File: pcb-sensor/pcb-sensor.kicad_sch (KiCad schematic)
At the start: 28 parts, among them J1 Conn_02x06_Counter_Clockwise, J2 Conn_01x03, J3 Conn_01x01, J4 Conn_01x05, J5 Conn_01x02, J6 Conn_01x03, J7 Conn_01x01, J8 Conn_01x01, U1 LM340MP, U2 SFH617A-1, U4 SFH617A-1

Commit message: resolves #37: optocoupler footprint
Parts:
- U2, U4: value SFH617A-1 -> SFH617A-2X009T; footprint Package_SO:SOP-4_4.4x2.6mm_P1.27mm -> Package_DIP:SMDIP-4_W7.62mm; symbol Isolator:SFH617A-1 -> Isolator:SFH617A-2X009T
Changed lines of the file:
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@@
     (pin "1")
   )
-  (symbol (lib_id "Isolator:SFH617A-1") (at 184.15 88.9 0) (unit 1)
+  (symbol (lib_id "Isolator:SFH617A-2X009T") (at 184.15 88.9 0) (unit 1)
     (in_bom yes) (on_board yes)
     (property "Reference" "U2" (id 0) (at 184.15 82.9818 0))
-    (property "Value" "SFH617A-1" (id 1) (at 184.15 93.98 0))
-    (property "Footprint" "Package_SO:SOP-4_4.4x2.6mm_P1.27mm" (id 2) (at 179.07 93.98 0)
-      (effects (font (size 1.27 1.27) italic) (justify left) hide)
-    )
-    (property "Datasheet" "http://www.vishay.com/docs/83740/sfh617a.pdf" (id 3) (at 184.15 88.9 0)
-      (effects (font (size 1.27 1.27)) (justify left) hide)
+    (property "Value" "SFH617A-2X009T" (id 1) (at 184.15 93.98 0))
+    (property "Footprint" "Package_DIP:SMDIP-4_W7.62mm" (id 2) (at 184.15 96.52 0)
+      (effects (font (size 1.27 1.27)) hide)
+    )
+    (property "Datasheet" "http://www.vishay.com/docs/83740/sfh617a.pdf" (id 3) (at 175.26 81.28 0)
+      (effects (font (size 1.27 1.27)) hide)
     )
     (pin "1")
@@
     (pin "4")
   )
-  (symbol (lib_id "Isolator:SFH617A-1") (at 251.46 90.17 0) (unit 1)
+  (symbol (lib_id "Isolator:SFH617A-2X009T") (at 251.46 90.17 0) (unit 1)
     (in_bom yes) (on_board yes)
     (property "Reference" "U4" (id 0) (at 251.46 84.2518 0))
-    (property "Value" "SFH617A-1" (id 1) (at 251.46 95.25 0))
-    (property "Footprint" "Package_SO:SOP-4_4.4x2.6mm_P1.27mm" (id 2) (at 246.38 95.25 0)
-      (effects (font (size 1.27 1.27) italic) (justify left) hide)
-    )
-    (property "Datasheet" "http://www.vishay.com/docs/83740/sfh617a.pdf" (id 3) (at 251.46 90.17 0)
-      (effects (font (size 1.27 1.27)) (justify left) hide)
+    (property "Value" "SFH617A-2X009T" (id 1) (at 251.46 95.25 0))
+    (property "Footprint" "Package_DIP:SMDIP-4_W7.62mm" (id 2) (at 251.46 97.79 0)
+      (effects (font (size 1.27 1.27)) hide)
+    )
+    (property "Datasheet" "http://www.vishay.com/docs/83740/sfh617a.pdf" (id 3) (at 242.57 82.55 0)
+      (effects (font (size 1.27 1.27)) hide)
     )
     (pin "1")
@@
     )
     (path "/00000000-0000-0000-0000-000061cdde7e"
-      (reference "U2") (unit 1) (value "SFH617A-1") (footprint "Package_SO:SOP-4_4.4x2.6mm_P1.27mm")
+      (reference "U2") (unit 1) (value "SFH617A-2X009T") (footprint "Package_DIP:SMDIP-4_W7.62mm")
     )
     (path "/00000000-0000-0000-0000-000061ceb6aa"
-      (reference "U4") (unit 1) (value "SFH617A-1") (footprint "Package_SO:SOP-4_4.4x2.6mm_P1.27mm")
-    )
-  )
+      (reference "U4") (unit 1) (value "SFH617A-2X009T") (footprint "Package_DIP:SMDIP-4_W7.62mm")
+    )
+  )

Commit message: resolves #43: reduce hall effect sensor pull up to remove noise
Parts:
- R11: value 10k -> 1k
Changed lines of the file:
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@@
       (effects (font (size 1.27 1.27)) (justify left))
     )
-    (property "Value" "10k" (id 1) (at 263.398 139.573 0)
+    (property "Value" "1k" (id 1) (at 263.398 139.573 0)
       (effects (font (size 1.27 1.27)) (justify left))
     )
@@
     )
     (path "/00000000-0000-0000-0000-0000616846c0"
-      (reference "R11") (unit 1) (value "10k") (footprint "Resistor_SMD:R_1206_3216Metric_Pad1.30x1.75mm_HandSolder")
+      (reference "R11") (unit 1) (value "1k") (footprint "Resistor_SMD:R_1206_3216Metric_Pad1.30x1.75mm_HandSolder")
     )
     (path "/00000000-0000-0000-0000-0000617d50e9"

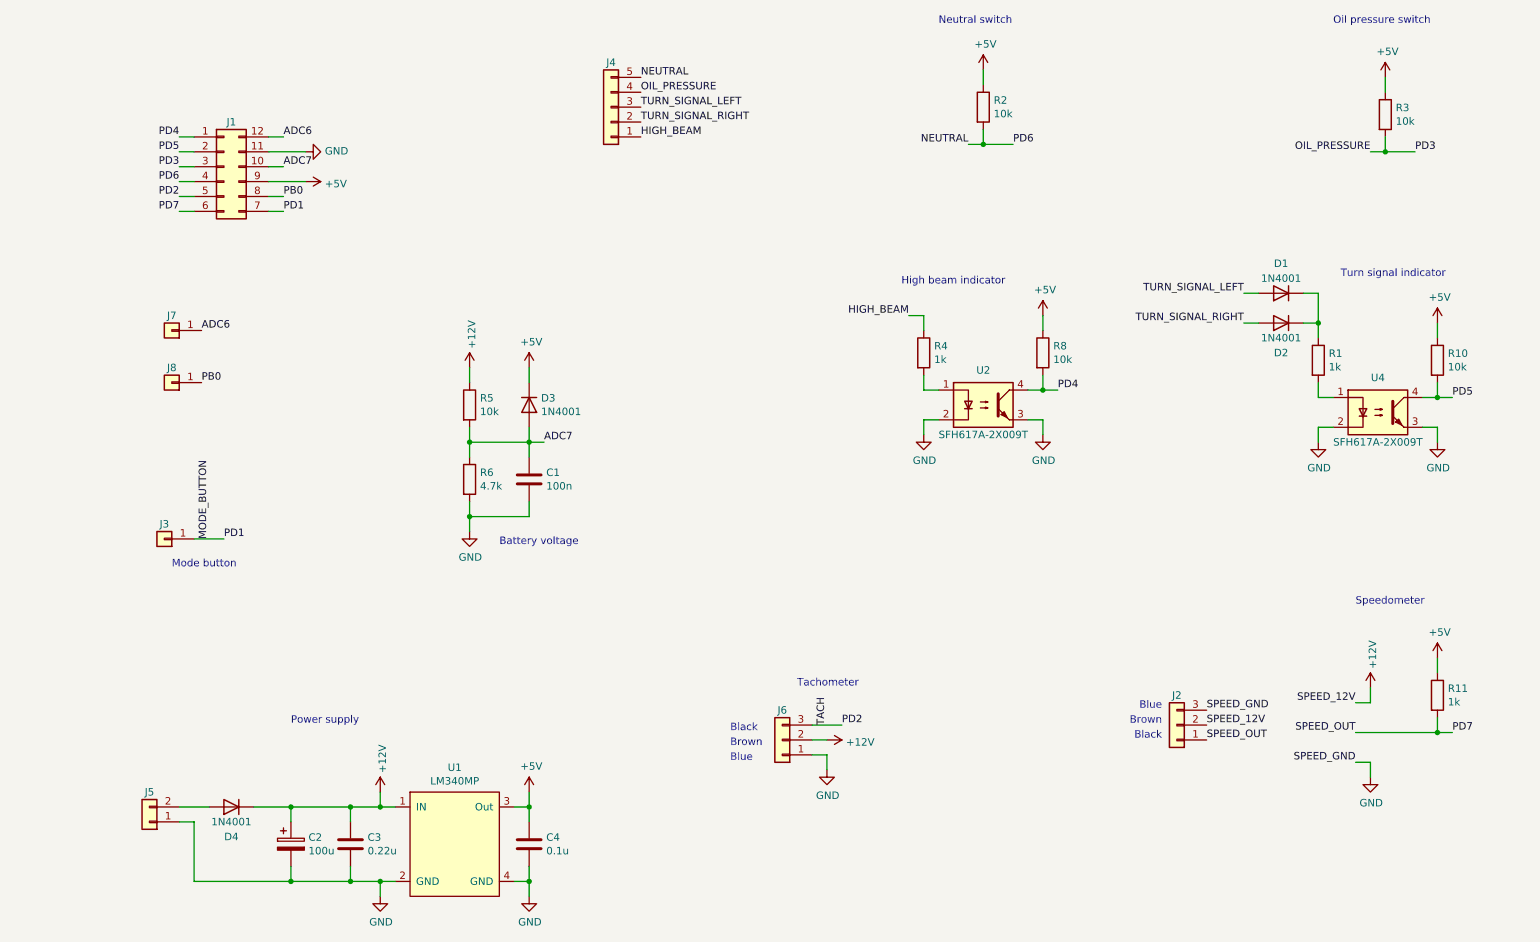
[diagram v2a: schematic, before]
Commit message: resolves #26: protection diodes
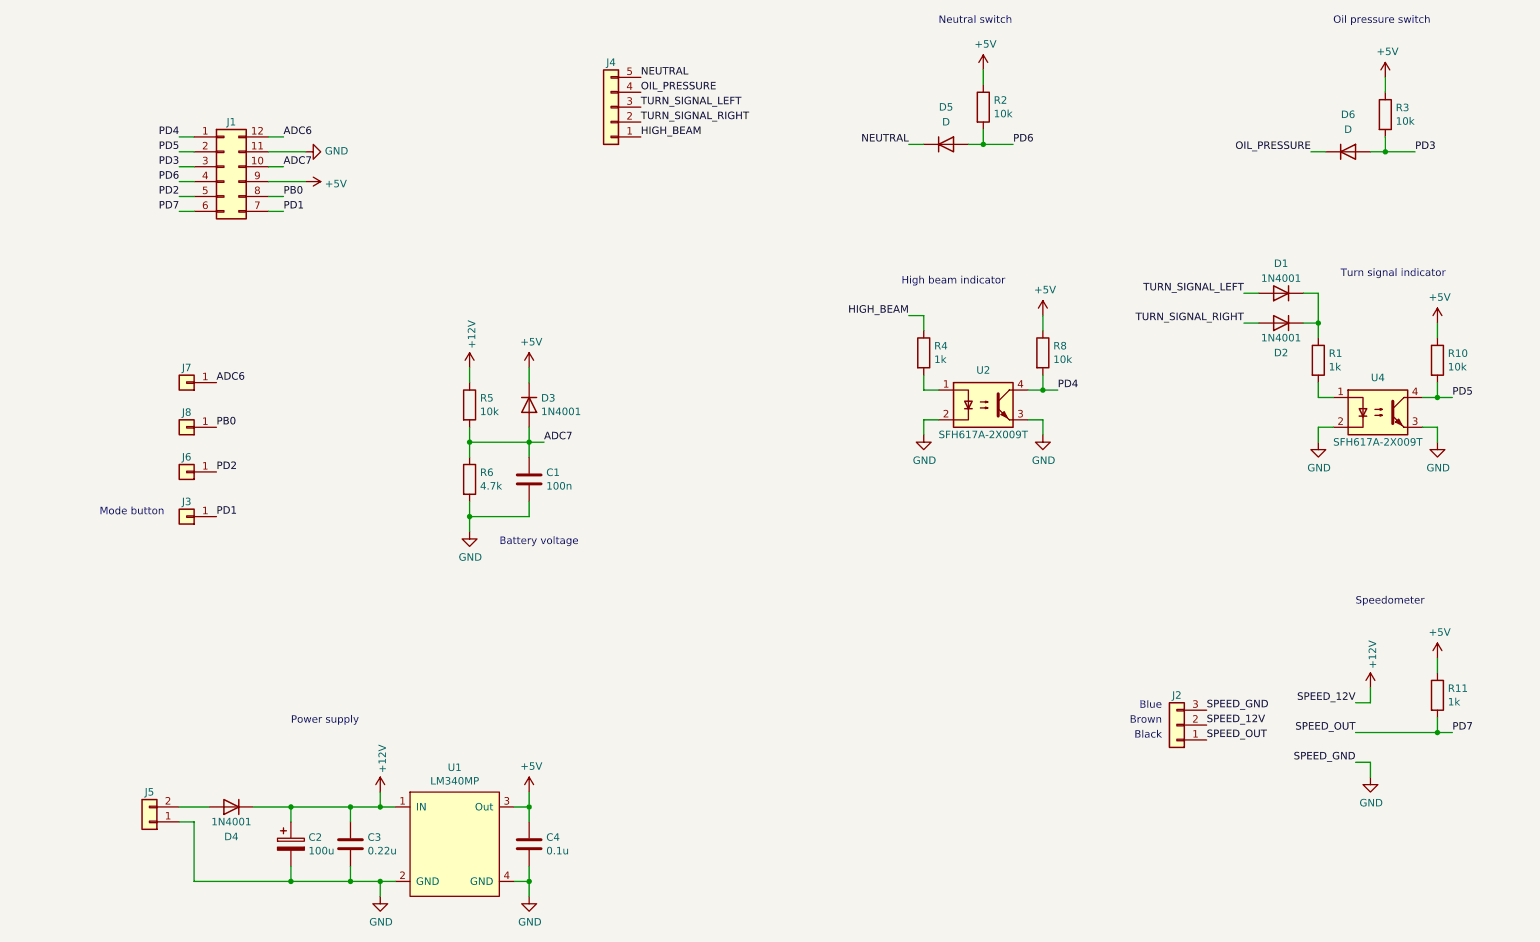
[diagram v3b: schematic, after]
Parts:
- removed J6: Conn_01x03, Connector_PinSocket_2.54mm:PinSocket_1x03_P2.54mm_Vertical, symbol Connector_Generic:Conn_01x03
- added D5, D6: D, Diode_SMD:D_1206_3216Metric_Pad1.42x1.75mm_HandSolder, symbol Device:D
- added J6: Conn_01x01, Connector_PinSocket_2.54mm:PinSocket_1x01_P2.54mm_Vertical, symbol Connector_Generic:Conn_01x01
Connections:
- net NEUTRAL: now also D5.1 (K); no longer J1.4 (Pin_4), R2.2
- net OIL_PRESSURE: now also D6.1 (K); no longer J1.3 (Pin_3), R3.2
- net PD2: now also J6.1 (Pin_1)
- net MODE_BUTTON renamed PD1
- new net PD3: D6.2 (A), J1.3 (Pin_3), R3.2
- new net PD6: D5.2 (A), J1.4 (Pin_4), R2.2
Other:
- note removed: "Tachometer"
- moved on the sheet: J3, J7, J8

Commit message: resolves #17: interrupt pin
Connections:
- net PD2: now also J2.1 (Pin_1), R11.2; no longer J6.1 (Pin_1)
- net PD7: now also J6.1 (Pin_1); no longer J2.1 (Pin_1), R11.2
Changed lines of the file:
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@@
     (effects (font (size 1.27 1.27)) (justify right bottom))
   )
-  (label "PD2" (at 53.34 100.33 0)
+  (label "PD7" (at 53.34 100.33 0)
     (effects (font (size 1.27 1.27)) (justify left bottom))
   )
@@
     (effects (font (size 1.27 1.27)) (justify right bottom))
   )
-  (label "PD7" (at 264.16 144.78 0)
+  (label "PD2" (at 264.16 144.78 0)
     (effects (font (size 1.27 1.27)) (justify left bottom))
   )

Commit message: resolves #46: mode button connector
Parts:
- removed J3: Conn_01x01, Connector_PinSocket_2.54mm:PinSocket_1x01_P2.54mm_Vertical, symbol Connector_Generic:Conn_01x01
- added J9: Conn_01x02_Male, Connector_JST:JST_PH_S2B-PH-K_1x02_P2.00mm_Horizontal, symbol Connector:Conn_01x02_Male
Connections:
- net GND: now also J9.2 (Pin_2)
- net PD1: now also J9.1 (Pin_1)
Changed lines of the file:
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@@
+    (stroke (width 0) (type default) (color 0 0 0 0))
+  )
+  (wire (pts (xy 154.94 132.08) (xy 157.48 132.08))
     (stroke (width 0) (type default) (color 0 0 0 0))
   )
@@
     (stroke (width 0) (type default) (color 0 0 0 0))
   )
+  (wire (pts (xy 154.94 134.62) (xy 157.48 134.62))
+    (stroke (width 0) (type default) (color 0 0 0 0))
+  )
   (text "Neutral switch" (at 176.53 24.13 0)
     (effects (font (size 1.27 1.27)) (justify left bottom))
@@
     (effects (font (size 1.27 1.27)) (justify left bottom))
   )
-  (text "Mode button" (at 44.45 107.95 180)
+  (text "Mode button" (at 156.21 139.7 180)
     (effects (font (size 1.27 1.27)) (justify right bottom))
   )
@@
     (effects (font (size 1.27 1.27)) (justify left bottom))
   )
-  (label "PD1" (at 53.34 107.95 0)
-    (effects (font (size 1.27 1.27)) (justify left bottom))
-  )
   (label "PD1" (at 64.77 55.88 0)
     (effects (font (size 1.27 1.27)) (justify left bottom))
@@
   (label "PD3" (at 46.99 48.26 180)
     (effects (font (size 1.27 1.27)) (justify right bottom))
+  )
+  (label "PD1" (at 157.48 132.08 0)
+    (effects (font (size 1.27 1.27)) (justify left bottom))
   )
   (symbol (lib_id "Connector_Generic:Conn_02x06_Counter_Clockwise") (at 54.61 48.26 0) (unit 1)
@@
     (pin "4")
   )
-  (symbol (lib_id "Connector_Generic:Conn_01x01") (at 48.26 107.95 180) (unit 1)
-    (in_bom yes) (on_board yes)
-    (property "Reference" "J3" (id 0) (at 48.26 105.41 0))
-    (property "Value" "Conn_01x01" (id 1) (at 50.3428 104.5464 0)
-      (effects (font (size 1.27 1.27)) hide)
-    )
-    (property "Footprint" "Connector_PinSocket_2.54mm:PinSocket_1x01_P2.54mm_Vertical" (id 2) (at 48.26 107.95 0)
-      (effects (font (size 1.27 1.27)) hide)
-    )
-    (property "Datasheet" "~" (id 3) (at 48.26 107.95 0)
-      (effects (font (size 1.27 1.27)) hide)
-    )
-    (pin "1")
-  )
   (symbol (lib_id "Connector_Generic:Conn_01x01") (at 48.26 92.71 180) (unit 1)
     (in_bom yes) (on_board yes)
@@
     (pin "2")
   )
+  (symbol (lib_id "power:GND") (at 157.48 134.62 90) (unit 1)
+    (in_bom yes) (on_board yes)
+    (property "Reference" "#PWR0105" (id 0) (at 163.83 134.62 0)
+      (effects (font (size 1.27 1.27)) hide)
+    )
+    (property "Value" "GND" (id 1) (at 160.7312 134.493 90)
+      (effects (font (size 1.27 1.27)) (justify right))
+    )
+    (property "Footprint" "" (id 2) (at 157.48 134.62 0)
+      (effects (font (size 1.27 1.27)) hide)
+    )
+    (property "Datasheet" "" (id 3) (at 157.48 134.62 0)
+      (effects (font (size 1.27 1.27)) hide)
+    )
+    (pin "1")
+  )
   (symbol (lib_id "Connector_Generic:Conn_01x01") (at 48.26 100.33 180) (unit 1)
     (in_bom yes) (on_board yes)
@@
     )
     (pin "1")
+  )
+  (symbol (lib_id "Connector:Conn_01x02_Male") (at 149.86 132.08 0) (unit 1)
+    (in_bom yes) (on_board yes) (fields_autoplaced)
+    (property "Reference" "J9" (id 0) (at 150.495 127 0))
+    (property "Value" "Conn_01x02_Male" (id 1) (at 150.495 129.54 0))
+    (property "Footprint" "Connector_JST:JST_PH_S2B-PH-K_1x02_P2.00mm_Horizontal" (id 2) (at 149.86 132.08 0)
+      (effects (font (size 1.27 1.27)) hide)
+    )
+    (property "Datasheet" "~" (id 3) (at 149.86 132.08 0)
+      (effects (font (size 1.27 1.27)) hide)
+    )
+    (pin "1")
+    (pin "2")
   )
   (sheet_instances
@@
       (reference "#PWR0104") (unit 1) (value "+12V") (footprint "")
     )
+    (path "/8fc9b42a-be9e-4b68-b6b5-47e33fba5f6c"
+      (reference "#PWR0105") (unit 1) (value "GND") (footprint "")
+    )
     (path "/00000000-0000-0000-0000-00006187b8d1"
       (reference "#PWR0106") (unit 1) (value "GND") (footprint "")
@@
       (reference "J2") (unit 1) (value "Conn_01x03") (footprint "Connector_PinSocket_2.54mm:PinSocket_1x03_P2.54mm_Vertical")
     )
-    (path "/00000000-0000-0000-0000-000061df2613"
-      (reference "J3") (unit 1) (value "Conn_01x01") (footprint "Connector_PinSocket_2.54mm:PinSocket_1x01_P2.54mm_Vertical")
-    )
     (path "/00000000-0000-0000-0000-000061af42fb"
       (reference "J4") (unit 1) (value "Conn_01x05") (footprint "Connector_PinSocket_2.54mm:PinSocket_1x05_P2.54mm_Vertical")
@@
       (reference "J8") (unit 1) (value "Conn_01x01") (footprint "Connector_PinSocket_2.54mm:PinSocket_1x01_P2.54mm_Vertical")
     )
+    (path "/e17ef7e8-7ef3-48c9-a4ab-39b37df20ec3"
+      (reference "J9") (unit 1) (value "Conn_01x02_Male") (footprint "Connector_JST:JST_PH_S2B-PH-K_1x02_P2.00mm_Horizontal")
+    )
     (path "/00000000-0000-0000-0000-0000618559fe"

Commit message: update layout
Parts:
- removed J2: Conn_01x03, Connector_PinSocket_2.54mm:PinSocket_1x03_P2.54mm_Vertical, symbol Connector_Generic:Conn_01x03
- removed J4: Conn_01x05, Connector_PinSocket_2.54mm:PinSocket_1x05_P2.54mm_Vertical, symbol Connector_Generic:Conn_01x05
- removed J5: Conn_01x02, Connector_PinSocket_2.54mm:PinSocket_1x02_P2.54mm_Vertical, symbol Connector_Generic:Conn_01x02
- removed J6, J7, J8: Conn_01x01, Connector_PinSocket_2.54mm:PinSocket_1x01_P2.54mm_Vertical, symbol Connector_Generic:Conn_01x01
- removed J9: Conn_01x02_Male, Connector_JST:JST_PH_S2B-PH-K_1x02_P2.00mm_Horizontal, symbol Connector:Conn_01x02_Male
- added J2, J5: Conn_01x02_Male, Connector_JST:JST_PH_S2B-PH-K_1x02_P2.00mm_Horizontal, symbol Connector:Conn_01x02_Male
- added J3, J6: Conn_01x03_Male, Connector_JST:JST_PH_S3B-PH-K_1x03_P2.00mm_Horizontal, symbol Connector:Conn_01x03_Male
- added J4: Conn_01x05_Male, Connector_JST:JST_PH_S5B-PH-K_1x05_P2.00mm_Horizontal, symbol Connector:Conn_01x05_Male
- added R7: 47k, Resistor_SMD:R_1206_3216Metric_Pad1.30x1.75mm_HandSolder, symbol Device:R
- added R9: 1k, Resistor_SMD:R_1206_3216Metric_Pad1.30x1.75mm_HandSolder, symbol Device:R
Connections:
- net +12V: now also J3.1 (Pin_1), J6.1 (Pin_1)
- net +5V: now also R7.1, R9.1
- net ADC6: now also J2.1 (Pin_1), R7.2
- net GND: now also J2.2 (Pin_2), J3.3 (Pin_3), J5.2 (Pin_2), J6.3 (Pin_3)
- net HIGH_BEAM: now also J4.5 (Pin_5)
- net NEUTRAL: now also J4.1 (Pin_1)
- net OIL_PRESSURE: now also J4.2 (Pin_2)
- net PD1: now also D6.2 (A), R3.2
- net PD2: now also J6.2 (Pin_2)
- net PD3: now also J3.2 (Pin_2), R9.2; no longer D6.2 (A), R3.2
- net TURN_SIGNAL_LEFT: now also J4.3 (Pin_3)
- net TURN_SIGNAL_RIGHT: now also J4.4 (Pin_4)
- net at D4.2 (A): now also J5.1 (Pin_1)
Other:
- note added: "Tachometer"
- note added: "Temperature"
- note removed: "Mode button"
- moved on the sheet: C1, C2, C3, C4, D1, D2, D3, D4, D5, J1, R1, R10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

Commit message: update pcb layouts
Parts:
- removed J2, J5: Conn_01x02_Male, Connector_JST:JST_PH_S2B-PH-K_1x02_P2.00mm_Horizontal, symbol Connector:Conn_01x02_Male
- removed J3, J6: Conn_01x03_Male, Connector_JST:JST_PH_S3B-PH-K_1x03_P2.00mm_Horizontal, symbol Connector:Conn_01x03_Male
- removed J4: Conn_01x05_Male, Connector_JST:JST_PH_S5B-PH-K_1x05_P2.00mm_Horizontal, symbol Connector:Conn_01x05_Male
- added J7: Conn_02x08_Top_Bottom, Connector_Molex:Molex_Mini-Fit_Jr_5566-16A_2x08_P4.20mm_Vertical, symbol Connector_Generic:Conn_02x08_Top_Bottom
- J1: footprint Connector_PinSocket_2.54mm:PinSocket_2x06_P2.54mm_Vertical -> Connector_PinSocket_2.00mm:PinSocket_2x06_P2.00mm_Vertical
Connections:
- net +12V: now also J7.4 (Pin_4), J7.6 (Pin_6)
- net ADC6: now also C1.1, D3.2 (A), R5.2, R6.1; no longer R7.2
- net ADC7: now also R7.2, J7.2 (Pin_2); no longer C1.1, D3.2 (A), R5.2, R6.1
- net GND: now also J7.1 (Pin_1), J7.10 (Pin_10), J7.11 (Pin_11), J7.13 (Pin_13)
- net PD1: no longer D6.2 (A), R3.2
- net PD2: now also R9.2, J7.3 (Pin_3); no longer R11.2
- net PD3: now also R11.2, J7.5 (Pin_5); no longer R9.2
- net PD4: now also D5.2 (A), R2.2; no longer R8.2, U2.4
- net PD5: now also D6.2 (A), R3.2; no longer R10.2, U4.4
- net PD6: now also R10.2, U4.4; no longer D5.2 (A), R2.2
- net PD7: now also R8.2, U2.4
- net Power 12V: now reaches D4.2 (A)
- net Power 12V: now also J7.9 (Pin_9)
- net HIGH_BEAM renamed High Beam
- net High Beam: now also J7.7 (Pin_7)
- net NEUTRAL renamed Neutral
- net Neutral: now also J7.14 (Pin_14)
- net OIL_PRESSURE renamed Oil Pressure
- net Oil Pressure: now also J7.15 (Pin_15)
- net TURN_SIGNAL_LEFT renamed Left Turn
- net Left Turn: now also J7.16 (Pin_16)
- net TURN_SIGNAL_RIGHT renamed Right Turn
- net Right Turn: now also J7.8 (Pin_8)
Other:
- note added: "TODO: check capacitor / battery cell clearance"
- note added: "Temperature / Wideband"
- note removed: "Black"
- note removed: "Blue"
- note removed: "Brown"
- note removed: "Temperature"
- moved on the sheet: C1, C2, C3, C4, D1, D2, D3, D4, D5, D6, J1, R1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

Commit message: v1.3 last minute changes
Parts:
- added Q?: Q_NPN_BCE, symbol Device:Q_NPN_BCE
- C3: value 0.22u -> 220n
- C4: value 0.1u -> 100n
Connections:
- net +12V: now also Q?.2 (C)
- net PD2: now also Q?.1 (B), Q?.3 (E)
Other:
- note added: "Unused"
- note removed: "TODO: check capacitor / battery cell clearance"
- moved on the sheet: J1, R7
